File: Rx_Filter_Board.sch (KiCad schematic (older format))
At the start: 62 parts, among them K1 HK4100, K15 HK4100, K2 HK4100, K8 HK4100, K9 HK4100, P1 BNC, P2 BNC, P3 BNC, P4 BNC, P5 CONN_01X03, P6 CONN_01X03, P7 CONN_01X05, P8 CONN_01X04, U1 ULN2003, U2 74HC238

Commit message: First cut at filter circuit
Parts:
- removed C7, C8, C? (x8): C, symbol C
- removed GS1, GS2: GS2, Connect:GS2, symbol GS2
- removed P3: BNC, Connectors_G:rfconnectorB, symbol BNC
- removed P7: CONN_01X05, Pin_Headers:Pin_Header_Angled_1x05, symbol CONN_01X05-RESCUE-SwitchingBrd
- removed P8: CONN_01X04, Pin_Headers:Pin_Header_Angled_1x04, symbol CONN_01X04
- removed R1: 10k, Resistors_SMD:R_1206_HandSoldering, symbol R-RESCUE-SwitchingBrd
- removed U2: 74HC238, Sockets_DIP:DIP-16__300_ELL, symbol 74LS138
- added C10, C11, C12, C18, C2, C21, C23, C25, C3, C4: C, symbol C
- added D1, D2, D3, D4, D5, D6: LED, symbol Led_Small
- added K10, K5: HK4100, relays_G:HK4100, symbol HK4100
- added P6: CONN_01X02, symbol CONN_01X02
- added P7: CONN_01X07, symbol CONN_01X07
- added R1, R2, R3, R4, R5, R6: 1k5, symbol R
- gave numbers to parts that had none: 23
- renumbered C1 to C22, C13 to C24, C25 to C26, C2 to C6, K8 to K11, K15 to K12, K1 to K13, K9 to K7, L7 to L10, L8 to L6, L1 to L9, P4 to P2, P2 to P3, P5 to P4, P6 to P5
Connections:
- net labels removed: +5v, VCC
- wire segments 167 -> 241
- no-connect marks 9 -> 13
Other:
- note added: "15/10 M"
- note added: "20/17M"
- note added: "40/30 M"
- note added: "Antenna\nvia TX Filters"
- note added: "Through Filter"
- note added: "To Receiver\nvia Rx Filters"
- note added: "To\nReceiver\nInput"
- note added: "To\nTransmitter\nOutput"
- note removed: "Antenna"
- note removed: "Break Link if using\nchangeover relay"
- note removed: "Connect Link if using\nchangeover relay"
- note removed: "OPTIONAL\nAntenna C/O Relay"
- note removed: "To Receiver"
- note removed: "To Transmitter\nOutput"
- note removed: "Transmit Antenna"
- moved on the sheet: C1, C13, C14, C15, C16, C17, C22, C24, C26, C27, C5, C6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

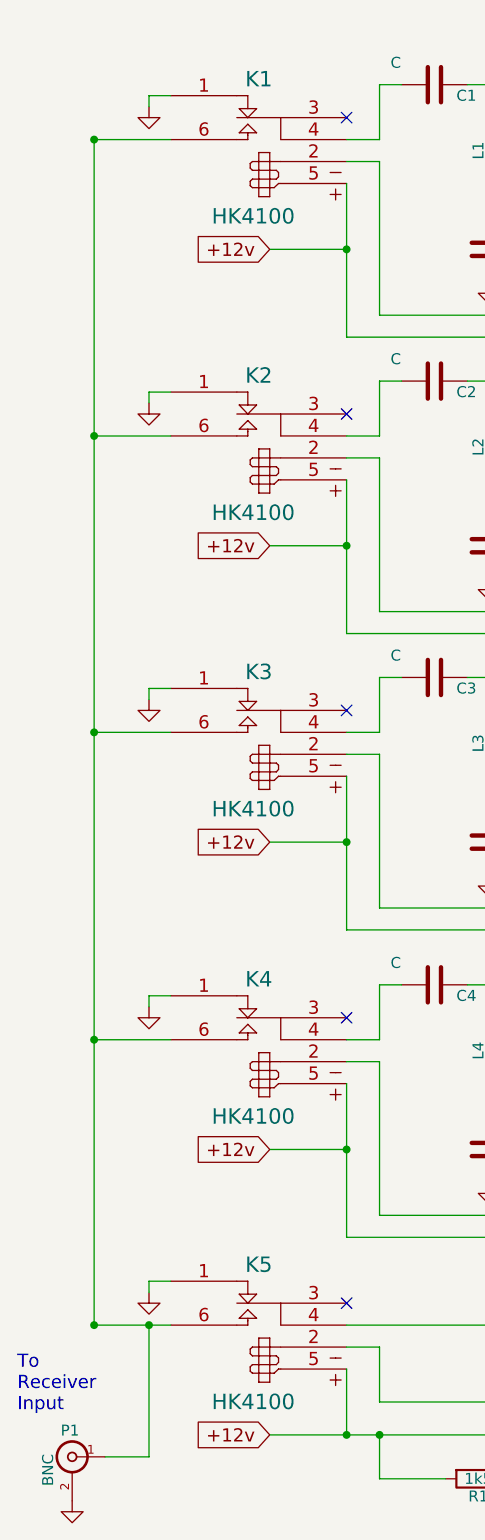
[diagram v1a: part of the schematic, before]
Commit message: Some layout tweaks only
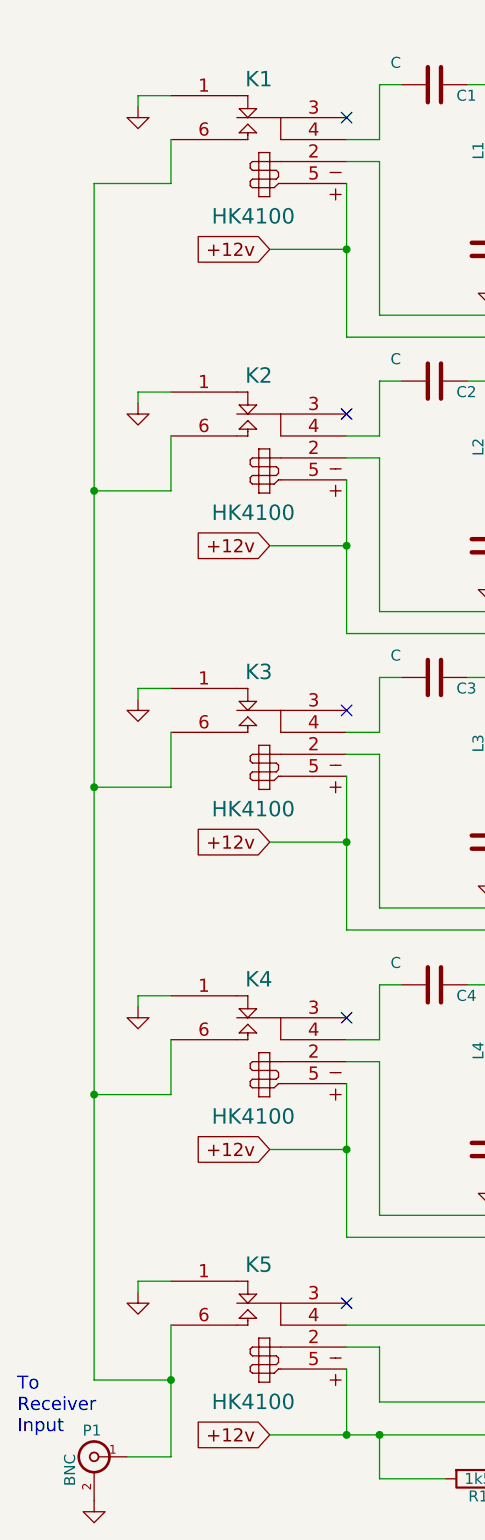
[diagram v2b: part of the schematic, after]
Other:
- moved on the sheet: P1
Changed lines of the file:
@@
 LIBS:contrib
 LIBS:valves
+LIBS:relays_G
 LIBS:Rx_Filter_Board-rescue
 LIBS:Rx_Filter_Board-cache
@@
 L GND #PWR3
 U 1 1 57ECDE45
-P 1450 2450
-F 0 "#PWR3" H 1450 2200 50  0001 C CNN
-F 1 "GND" H 1450 2300 50  0001 C CNN
-F 2 "" H 1450 2450 50  0000 C CNN
-F 3 "" H 1450 2450 50  0001 C CNN
-	1    1450 2450
+P 1400 2450
+F 0 "#PWR3" H 1400 2200 50  0001 C CNN
+F 1 "GND" H 1400 2300 50  0001 C CNN
+F 2 "" H 1400 2450 50  0000 C CNN
+F 3 "" H 1400 2450 50  0001 C CNN
+	1    1400 2450
 	1    0    0    -1
 $EndComp
@@
 L GND #PWR4
 U 1 1 57ECE8C7
-P 1450 3800
-F 0 "#PWR4" H 1450 3550 50  0001 C CNN
-F 1 "GND" H 1450 3650 50  0001 C CNN
-F 2 "" H 1450 3800 50  0000 C CNN
-F 3 "" H 1450 3800 50  0001 C CNN
-	1    1450 3800
+P 1400 3800
+F 0 "#PWR4" H 1400 3550 50  0001 C CNN
+F 1 "GND" H 1400 3650 50  0001 C CNN
+F 2 "" H 1400 3800 50  0000 C CNN
+F 3 "" H 1400 3800 50  0001 C CNN
+	1    1400 3800
 	1    0    0    -1
 $EndComp
@@
 L GND #PWR5
 U 1 1 57ECF3FF
-P 1450 5200
-F 0 "#PWR5" H 1450 4950 50  0001 C CNN
-F 1 "GND" H 1450 5050 50  0001 C CNN
-F 2 "" H 1450 5200 50  0000 C CNN
-F 3 "" H 1450 5200 50  0001 C CNN
-	1    1450 5200
+P 1400 5200
+F 0 "#PWR5" H 1400 4950 50  0001 C CNN
+F 1 "GND" H 1400 5050 50  0001 C CNN
+F 2 "" H 1400 5200 50  0000 C CNN
+F 3 "" H 1400 5200 50  0001 C CNN
+	1    1400 5200
 	1    0    0    -1
 $EndComp
@@
 L GND #PWR2
 U 1 1 57ECFAA1
-P 1450 1100
-F 0 "#PWR2" H 1450 850 50  0001 C CNN
-F 1 "GND" H 1450 950 50  0001 C CNN
-F 2 "" H 1450 1100 50  0000 C CNN
-F 3 "" H 1450 1100 50  0001 C CNN
-	1    1450 1100
+P 1400 1100
+F 0 "#PWR2" H 1400 850 50  0001 C CNN
+F 1 "GND" H 1400 950 50  0001 C CNN
+F 2 "" H 1400 1100 50  0000 C CNN
+F 3 "" H 1400 1100 50  0001 C CNN
+	1    1400 1100
 	1    0    0    -1
 $EndComp
@@
 L GND #PWR6
 U 1 1 57EDCC57
-P 1450 6500
-F 0 "#PWR6" H 1450 6250 50  0001 C CNN
-F 1 "GND" H 1450 6350 50  0001 C CNN
-F 2 "" H 1450 6500 50  0000 C CNN
-F 3 "" H 1450 6500 50  0001 C CNN
-	1    1450 6500
+P 1400 6500
+F 0 "#PWR6" H 1400 6250 50  0001 C CNN
+F 1 "GND" H 1400 6350 50  0001 C CNN
+F 2 "" H 1400 6500 50  0000 C CNN
+F 3 "" H 1400 6500 50  0001 C CNN
+	1    1400 6500
 	1    0    0    -1
 $EndComp
@@
 	5900 5550 7750 5550
 Wire Wire Line
-	1550 2600 1200 2600
-Connection ~ 1200 2600
+	1550 2850 1200 2850
+Connection ~ 1200 2850
 Wire Wire Line
 	5600 2850 5150 2850
@@
 	6100 5450 7750 5450
 Wire Wire Line
-	1550 2400 1450 2400
-Wire Wire Line
-	1450 2400 1450 2450
+	1550 2400 1400 2400
+Wire Wire Line
+	1400 2400 1400 2450
 Wire Wire Line
 	5150 2400 5350 2400
@@
 	4200 3950 4200 3700
 Wire Wire Line
-	1200 3950 1550 3950
-Connection ~ 1200 3950
+	1200 4200 1550 4200
+Connection ~ 1200 4200
 Wire Wire Line
 	5600 4200 5150 4200
 Wire Wire Line
-	1550 3750 1450 3750
-Wire Wire Line
-	1450 3750 1450 3800
+	1550 3750 1400 3750
+Wire Wire Line
+	1400 3750 1400 3800
 Wire Wire Line
 	5150 3750 5350 3750
@@
 	4200 5350 4200 5100
 Wire Wire Line
-	1200 5350 1550 5350
-Connection ~ 1200 5350
+	1200 5600 1550 5600
+Connection ~ 1200 5600
 Wire Wire Line
 	5600 5600 5150 5600
 Wire Wire Line
-	1550 5150 1450 5150
-Wire Wire Line
-	1450 5150 1450 5200
+	1550 5150 1400 5150
+Wire Wire Line
+	1400 5150 1400 5200
 Wire Wire Line
 	5150 5150 5350 5150
@@
 	4200 1250 4200 1000
 Wire Wire Line
-	1200 1250 1550 1250
-Connection ~ 1200 1250
+	1200 1450 1550 1450
 Wire Wire Line
 	5150 1450 5600 1450
@@
 	5600 1250 6600 1250
 Wire Wire Line
-	1550 1050 1450 1050
-Wire Wire Line
-	1450 1050 1450 1100
+	1550 1050 1400 1050
+Wire Wire Line
+	1400 1050 1400 1100
 Wire Wire Line
 	5150 1050 5350 1050
@@
 	10000 1250 10200 1250
 Wire Wire Line
-	1200 6650 1450 6650
-Wire Wire Line
-	1450 6650 1550 6650
-Connection ~ 1200 6650
+	1200 6900 1550 6900
 Wire Wire Line
 	5150 6650 5150 6900
 Wire Wire Line
-	1550 6450 1450 6450
-Wire Wire Line
-	1450 6450 1450 6500
+	1550 6450 1400 6450
+Wire Wire Line
+	1400 6450 1400 6500
 Wire Wire Line
 	5150 6450 5350 6450
@@
 Through Filter
 Wire Wire Line
-	1200 1250 1200 2600
-Wire Wire Line
-	1200 2600 1200 3950
-Wire Wire Line
-	1200 3950 1200 5350
-Wire Wire Line
-	1200 5350 1200 6650
+	1200 1450 1200 2850
+Wire Wire Line
+	1200 2850 1200 4200
+Wire Wire Line
+	1200 4200 1200 5600
+Wire Wire Line
+	1200 5600 1200 6900
 $Comp
 L BNC P1
 U 1 1 57EDF98C
-P 1100 7250
-F 0 "P1" H 1110 7370 50  0000 C CNN
-F 1 "BNC" V 1210 7190 50  0000 C CNN
-F 2 "Connectors_G:rfconnectorB" H 1100 7250 60  0001 C CNN
-F 3 "" H 1100 7250 60  0000 C CNN
-	1    1100 7250
+P 1200 7250
+F 0 "P1" H 1210 7370 50  0000 C CNN
+F 1 "BNC" V 1310 7190 50  0000 C CNN
+F 2 "Connectors_G:rfconnectorB" H 1200 7250 60  0001 C CNN
+F 3 "" H 1200 7250 60  0000 C CNN
+	1    1200 7250
 	-1   0    0    -1
 $EndComp
-Text Notes 850  7050 0    60   ~ 0
+Text Notes 850  7150 0    60   ~ 0
 To\nReceiver\nInput
 $Comp
 L GND #PWR1
 U 1 1 57EDF993
-P 1100 7450
-F 0 "#PWR1" H 1100 7200 50  0001 C CNN
-F 1 "GND" H 1100 7300 50  0001 C CNN
-F 2 "" H 1100 7450 50  0000 C CNN
-F 3 "" H 1100 7450 50  0001 C CNN
-	1    1100 7450
+P 1200 7450
+F 0 "#PWR1" H 1200 7200 50  0001 C CNN
+F 1 "GND" H 1200 7300 50  0001 C CNN
+F 2 "" H 1200 7450 50  0000 C CNN
+F 3 "" H 1200 7450 50  0001 C CNN
+	1    1200 7450
 	1    0    0    -1
 $EndComp
@@
 	5600 6900 5150 6900
 Wire Wire Line
-	1250 7250 1450 7250
-Wire Wire Line
-	1450 7250 1450 6650
-Connection ~ 1450 6650
+	1550 7250 1350 7250
+Connection ~ 1550 6900
 NoConn ~ 6600 1350
 Wire Wire Line
@@
 	0    1    1    0
 $EndComp
+Wire Wire Line
+	1550 6650 1550 6900
+Wire Wire Line
+	1550 6900 1550 7250
+Wire Wire Line
+	1550 4200 1550 3950
+Wire Wire Line
+	1550 5600 1550 5350
+Wire Wire Line
+	1550 1450 1550 1250
+Wire Wire Line
+	1550 2600 1550 2850
 $EndSCHEMATC

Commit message: Board at 1st layout stage
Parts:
- removed D1: LED, symbol Led_Small
- removed P4, P5: CONN_01X03, Pin_Headers:Pin_Header_Angled_1x03, symbol CONN_01X03
- removed P7: CONN_01X07, symbol CONN_01X07
- removed R1: 1k5, symbol R
- added C10, C15, C20, C25, C5: C, Capacitors_SMD:C_1206_HandSoldering, symbol C
- added C33, C34, C35, C36, C37, C38, C39, C40, C41, C42, C43, C44, C45, C46, C47, C48, C49, C50, C51, C52, C53, C54, C55, C56: 0.1, Capacitors_SMD:C_1206_HandSoldering, symbol C
- added D5: LED, LEDs:LED_1206, symbol Led_Small
- added L10, L5: INDUCTOR, Toroids_T37:Toroid_T37_Vertical, symbol INDUCTOR
- added P4: CONN_01X08, Pin_Headers:Pin_Header_Straight_1x08, symbol CONN_01X08
- added R5: 1k5, Resistors_SMD:R_1206_HandSoldering, symbol R
- C1: value C -> 1500 pF; footprint (none) -> Capacitors_SMD:C_1206_HandSoldering
- C11: renamed from C9; value C -> 680 pF; footprint (none) -> Capacitors_SMD:C_1206_HandSoldering
- C12: renamed from C10; footprint (none) -> Capacitors_SMD:C_1206_HandSoldering
- C13: renamed from C11; footprint (none) -> Capacitors_SMD:C_1206_HandSoldering
- C14: renamed from C12; footprint (none) -> Capacitors_SMD:C_1206_HandSoldering
- C16: renamed from C13; value C -> 2700 pF; footprint (none) -> Capacitors_SMD:C_1206_HandSoldering
- C17: renamed from C14; footprint (none) -> Capacitors_SMD:C_1206_HandSoldering
- C18: renamed from C15; footprint (none) -> Capacitors_SMD:C_1206_HandSoldering
- C19: renamed from C16; footprint (none) -> Capacitors_SMD:C_1206_HandSoldering
- C2, C3, C4: footprint (none) -> Capacitors_SMD:C_1206_HandSoldering
- C21: renamed from C17; value C -> 2000 pF; footprint (none) -> Capacitors_SMD:C_1206_HandSoldering
- C22: renamed from C18; footprint (none) -> Capacitors_SMD:C_1206_HandSoldering
- C23: renamed from C19; footprint (none) -> Capacitors_SMD:C_1206_HandSoldering
- C24: renamed from C20; footprint (none) -> Capacitors_SMD:C_1206_HandSoldering
- C26: renamed from C21; value C -> 3000 pF; footprint (none) -> Capacitors_SMD:C_1206_HandSoldering
- C27: renamed from C22; value C -> .012 uF; footprint Resistors_Universal:Resistor_SMD+THTuniversal_0805to1206_RM10_HandSoldering -> Capacitors_SMD:C_1206_HandSoldering
- C28: renamed from C23; value C -> 1600 pF; footprint (none) -> Capacitors_SMD:C_1206_HandSoldering
- C29: renamed from C24; value C -> 2400 pF; footprint (none) -> Capacitors_SMD:C_1206_HandSoldering
- C30: renamed from C25; value C -> 1800 pF; footprint (none) -> Capacitors_SMD:C_1206_HandSoldering
- C31: renamed from C26; value C -> 3000 pF; footprint (none) -> Capacitors_SMD:C_1206_HandSoldering
- C32: renamed from C27; value C -> 6200 pF; footprint (none) -> Capacitors_SMD:C_1206_HandSoldering
- C6: renamed from C5; value C -> 8200 pF; footprint (none) -> Capacitors_SMD:C_1206_HandSoldering
- C7: renamed from C6; footprint (none) -> Capacitors_SMD:C_1206_HandSoldering
- C8: renamed from C7; footprint (none) -> Capacitors_SMD:C_1206_HandSoldering
- C9: renamed from C8; footprint (none) -> Capacitors_SMD:C_1206_HandSoldering
- D1: renamed from D2; footprint (none) -> LEDs:LED_1206
- D2: renamed from D3; footprint (none) -> LEDs:LED_1206
- D3: renamed from D4; footprint (none) -> LEDs:LED_1206
- D4: renamed from D5; footprint (none) -> LEDs:LED_1206
- D6: footprint (none) -> LEDs:LED_1206
- L1: value INDUCTOR -> 1.957uH; footprint (none) -> Toroids_T37:Toroid_T37_Vertical
- L11: renamed from L9; value INDUCTOR -> 3.967uH; footprint (none) -> Toroids_T37:Toroid_T37_Vertical
- L12: renamed from L10; value INDUCTOR -> 5.705uH; footprint (none) -> Toroids_T37:Toroid_T37_Vertical
- L13: renamed from L11; value INDUCTOR -> 6.067uH; footprint (none) -> Toroids_T37:Toroid_T37_Vertical
- L2, L3, L4: footprint (none) -> Toroids_T37:Toroid_T37_Vertical
- L6: renamed from L5; value INDUCTOR -> 2.545uH; footprint (none) -> Toroids_T37:Toroid_T37_Vertical
- L7: renamed from L6; footprint (none) -> Toroids_T37:Toroid_T37_Vertical
- L8: renamed from L7; footprint (none) -> Toroids_T37:Toroid_T37_Vertical
- L9: renamed from L8; footprint (none) -> Toroids_T37:Toroid_T37_Vertical
- P1, P2, P3: footprint Connectors_G:rfconnectorB -> Pin_Headers:Pin_Header_Straight_1x02
- P6: footprint (none) -> Pin_Headers:Pin_Header_Straight_1x02
- R1: renamed from R2; footprint (none) -> Resistors_SMD:R_1206_HandSoldering
- R2: renamed from R3; footprint (none) -> Resistors_SMD:R_1206_HandSoldering
- R3: renamed from R4; footprint (none) -> Resistors_SMD:R_1206_HandSoldering
- R4: renamed from R5; footprint (none) -> Resistors_SMD:R_1206_HandSoldering
- R6: footprint (none) -> Resistors_SMD:R_1206_HandSoldering
- U1: footprint Sockets_DIP:DIP-16__300_ELL -> Housings_DIP:DIP-16_W7.62mm_LongPads
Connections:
- net +12v: now also R1.1, R2.1, R3.1, C33.1, C34.1, C35.1, C36.1, C47.1, C48.1, C49.1, C50.1, C51.1, C53.1, C55.1, C56.1, R5.1
- net GND: now also C10.2, C20.2, C33.2, C34.2, C35.2, C36.2, C37.2, C38.2, C39.2, C40.2, C41.2, C42.2, C43.2, C44.2, C45.2, C46.2, C47.2, C48.2, C49.2, C50.2, C51.2, C52.2, C53.2, C54.2, C55.2, C56.2, P4.8 (P8)
- net at U1.1 (I1): now also P4.1 (P1)
- net at U1.10 (O7): now also K12.2
- net at K10.2, K5.2, U1.11 (O6): now also C41.1, C46.1, D5.1 (K)
- net at D4.1 (K), K4.2, K9.2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: now also C40.1, C45.1
- net at D3.1 (K), K3.2, K8.2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: now also C39.1, C44.1
- net at D2.1 (K), K2.2, K7.2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: now also C38.1, C43.1
- net at D1.1 (K), K1.2, K6.2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: now also C37.1, C42.1
- net at D6.1 (K), K11.2, K13.2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: now also C52.1, C54.1
- net at U1.2 (I2): now also P4.2 (P2)
- net at U1.3 (I3): now also P4.3 (P3)
- net at U1.4 (I4): now also P4.4 (P4)
- net at U1.5 (I5): now also P4.5 (P5)
- net at U1.6 (I6): now also P4.6 (P6)
- net ptt_In: now reaches U1.7 (I7)
- net ptt_In: now also P4.7 (P7)
- net at K12.1, K13.3: now also K13.4
- net at K10.6, K11.3, K6.6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: now also K11.4
- net at K2.3: now also C2.2, K2.4
- net at K7.3: now also C22.1, K7.4
- net at K3.3: now also C3.2, K3.4
- net at K8.3: now also C23.1, K8.4
- net at K4.3: now also C4.2, K4.4
- net at K9.3: now also C24.1, K9.4
- net at K1.3: now also C1.2, K1.4
- net at K6.3: now also C21.1, K6.4
- net at K5.3: now also K5.4, C5.2
- net at K10.4: now also K10.3, C25.1; no longer K5.4
- new net: C15.1, C25.2, L10.1
- new net: C20.1, L10.2
- new net: C15.2, C5.1, L5.1
- new net: C10.1, L5.2
- new net: D5.2 (A), R5.2
- no-connect marks 13 -> 0
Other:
- note added: "Placeholder"
- note removed: "PA Bias"
- note removed: "PTT"
- note removed: "Through Filter"
- moved on the sheet: C1, C11, C12, C13, C14, C16, C17, C18, C19, C2, C21, C22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

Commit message: A usable board at this point
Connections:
- net at C2.2, K2.4: no longer K2.3
- net at C22.1, K7.3: no longer K7.4
- net at C3.2, K3.3: no longer K3.4
- net at C23.1, K8.4: no longer K8.3
- net at C4.2, K4.4: no longer K4.3
- net at C24.1, K9.3: no longer K9.4
- net at C1.2, K1.3: no longer K1.4
- net at C21.1, K6.4: no longer K6.3
- net at C5.2, K5.3: no longer K5.4
- net at C25.1, K10.4: no longer K10.3
- no-connect marks 0 -> 9
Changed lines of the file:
@@
 $EndComp
 Wire Wire Line
-	2350 2300 2500 2300
-Wire Wire Line
-	2500 2300 2500 2150
+	2350 2400 2500 2400
+Wire Wire Line
+	2500 2400 2500 2150
 Wire Wire Line
 	4200 2300 4200 2150
@@
 	2350 2600 2350 3300
 Wire Wire Line
-	2350 3300 4350 3300
-Wire Wire Line
-	4350 3300 4350 2600
+	4350 3300 2350 3300
+Wire Wire Line
+	4350 2600 4350 3300
 Wire Wire Line
 	2000 2900 2350 2900
@@
 	2500 3650 2500 3500
 Wire Wire Line
-	4200 3650 4200 3500
+	4200 3750 4200 3500
 Wire Wire Line
 	1200 4000 1550 4000
@@
 	4200 3500 3900 3500
 Wire Wire Line
-	4350 3650 4200 3650
+	4350 3750 4200 3750
 Wire Wire Line
 	2350 3850 2650 3850
@@
 	2350 3950 2350 4650
 Wire Wire Line
-	2350 4650 4350 4650
-Wire Wire Line
-	4350 4650 4350 3950
+	4350 4650 2350 4650
+Wire Wire Line
+	4350 3950 4350 4650
 Wire Wire Line
 	2000 4250 2350 4250
 Connection ~ 2350 4250
 Wire Wire Line
-	2350 5050 2500 5050
-Wire Wire Line
-	2500 5050 2500 4900
+	2350 5150 2500 5150
+Wire Wire Line
+	2500 5150 2500 4900
 Wire Wire Line
 	4200 5050 4200 4900
@@
 	2350 5350 2350 6050
 Wire Wire Line
-	2350 6050 4350 6050
-Wire Wire Line
-	4350 6050 4350 5350
+	4350 6050 2350 6050
+Wire Wire Line
+	4350 5350 4350 6050
 Wire Wire Line
 	2000 5650 2350 5650
@@
 	2500 950  2500 800
 Wire Wire Line
-	4200 950  4200 800
+	4200 1050 4200 800
 Wire Wire Line
 	1200 1250 1550 1250
@@
 	4200 800  3900 800
 Wire Wire Line
-	4350 950  4200 950
+	4350 1050 4200 1050
 Wire Wire Line
 	2350 1150 2650 1150
@@
 	2350 1250 2350 1950
 Wire Wire Line
-	2350 1950 4350 1950
-Wire Wire Line
-	4350 1950 4350 1250
+	4350 1950 2350 1950
+Wire Wire Line
+	4350 1250 4350 1950
 Wire Wire Line
 	2000 1550 2350 1550
@@
 $EndComp
 Wire Wire Line
-	2350 6450 2500 6450
-Wire Wire Line
 	2500 6450 2500 6300
 Wire Wire Line
-	4200 6450 4200 6300
+	4200 6550 4200 6300
 Wire Wire Line
 	1550 6350 1400 6350
@@
 	4200 6300 3900 6300
 Wire Wire Line
-	4350 6450 4200 6450
-Wire Wire Line
 	2350 6650 2650 6650
 Wire Wire Line
@@
 	2350 6750 2350 7450
 Wire Wire Line
-	2350 7450 4350 7450
-Wire Wire Line
-	4350 7450 4350 6750
+	4350 7450 2350 7450
+Wire Wire Line
+	4350 6750 4350 7450
 Wire Wire Line
 	2000 7050 2350 7050
@@
 	2500 950  2350 950
 Wire Wire Line
-	2350 950  2350 1050
-Wire Wire Line
-	2350 2300 2350 2400
-Wire Wire Line
-	2350 3650 2350 3750
-Wire Wire Line
-	2350 5050 2350 5150
-Wire Wire Line
-	2350 6450 2350 6550
-Wire Wire Line
-	4350 6450 4350 6550
-Wire Wire Line
-	4350 5050 4350 5150
-Wire Wire Line
-	4350 3650 4350 3750
-Wire Wire Line
-	4350 2300 4350 2400
-Wire Wire Line
-	4350 950  4350 1050
-Wire Wire Line
 	6600 1250 6600 1350
 Wire Wire Line
@@
 $EndComp
 Connection ~ 2150 2900
+Wire Wire Line
+	4200 6550 4350 6550
+NoConn ~ 4350 6450
+Wire Wire Line
+	2350 6450 2500 6450
+NoConn ~ 2350 6550
+NoConn ~ 4350 5150
+NoConn ~ 2350 5050
+NoConn ~ 2350 3750
+NoConn ~ 4350 3650
+NoConn ~ 4350 2400
+NoConn ~ 2350 2300
+NoConn ~ 2350 1050
 $EndSCHEMATC
